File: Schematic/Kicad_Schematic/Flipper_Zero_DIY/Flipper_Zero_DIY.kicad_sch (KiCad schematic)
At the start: 0 parts

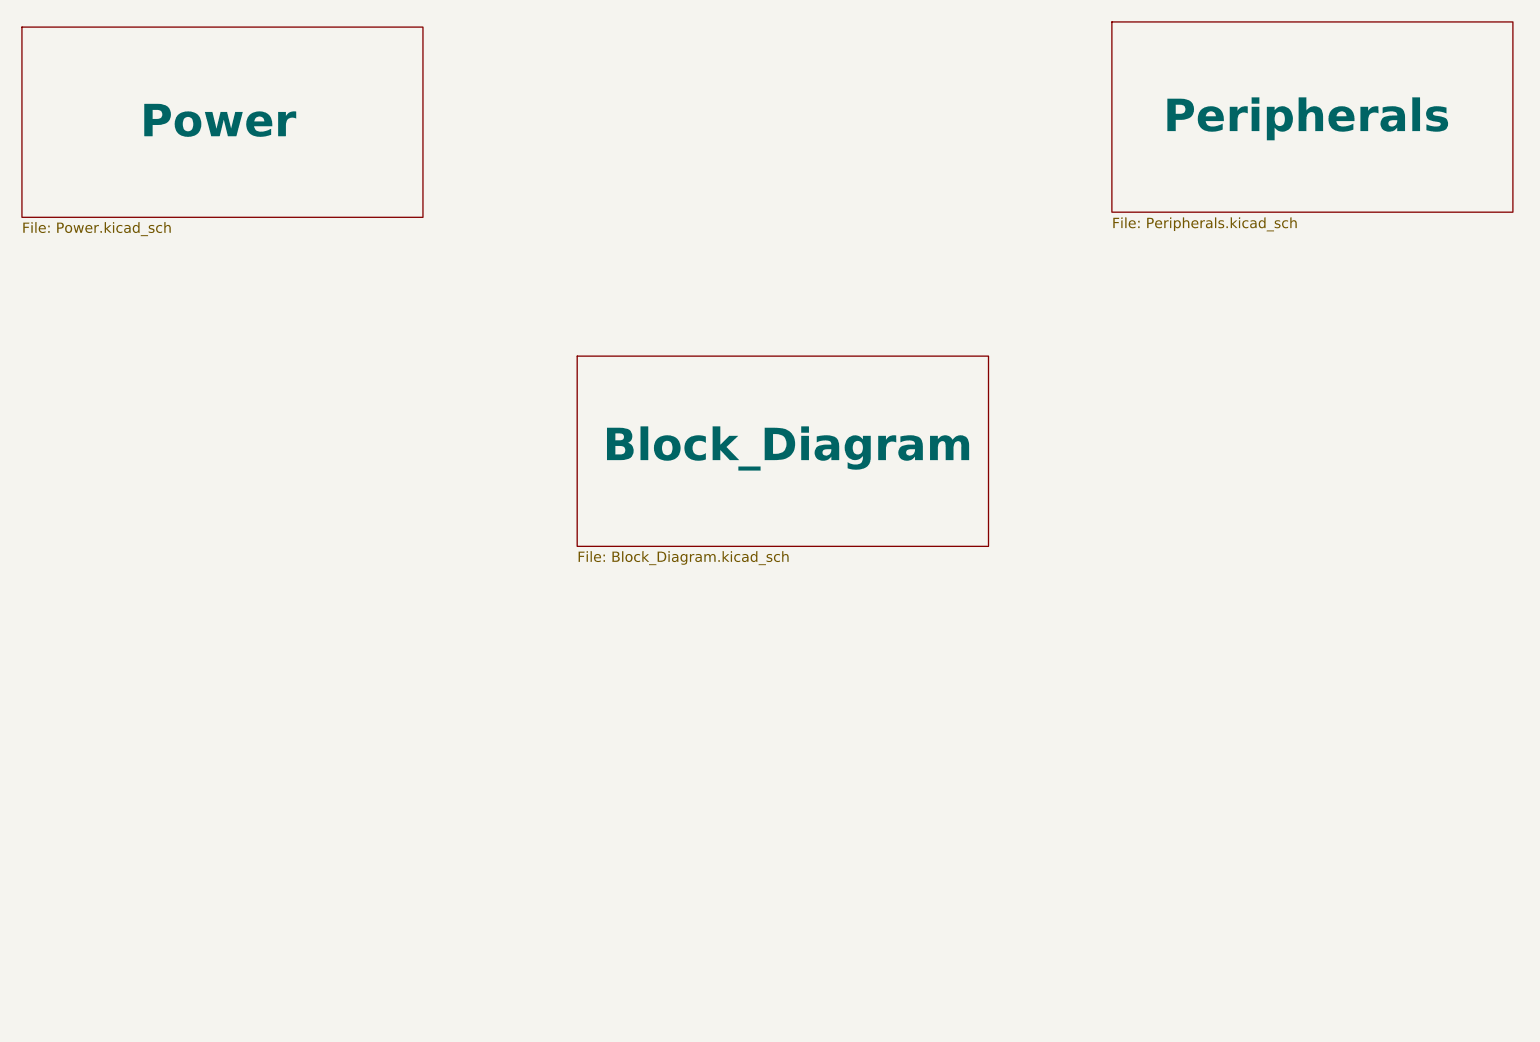
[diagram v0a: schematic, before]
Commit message: finished MCU schematic & new design of front shematic
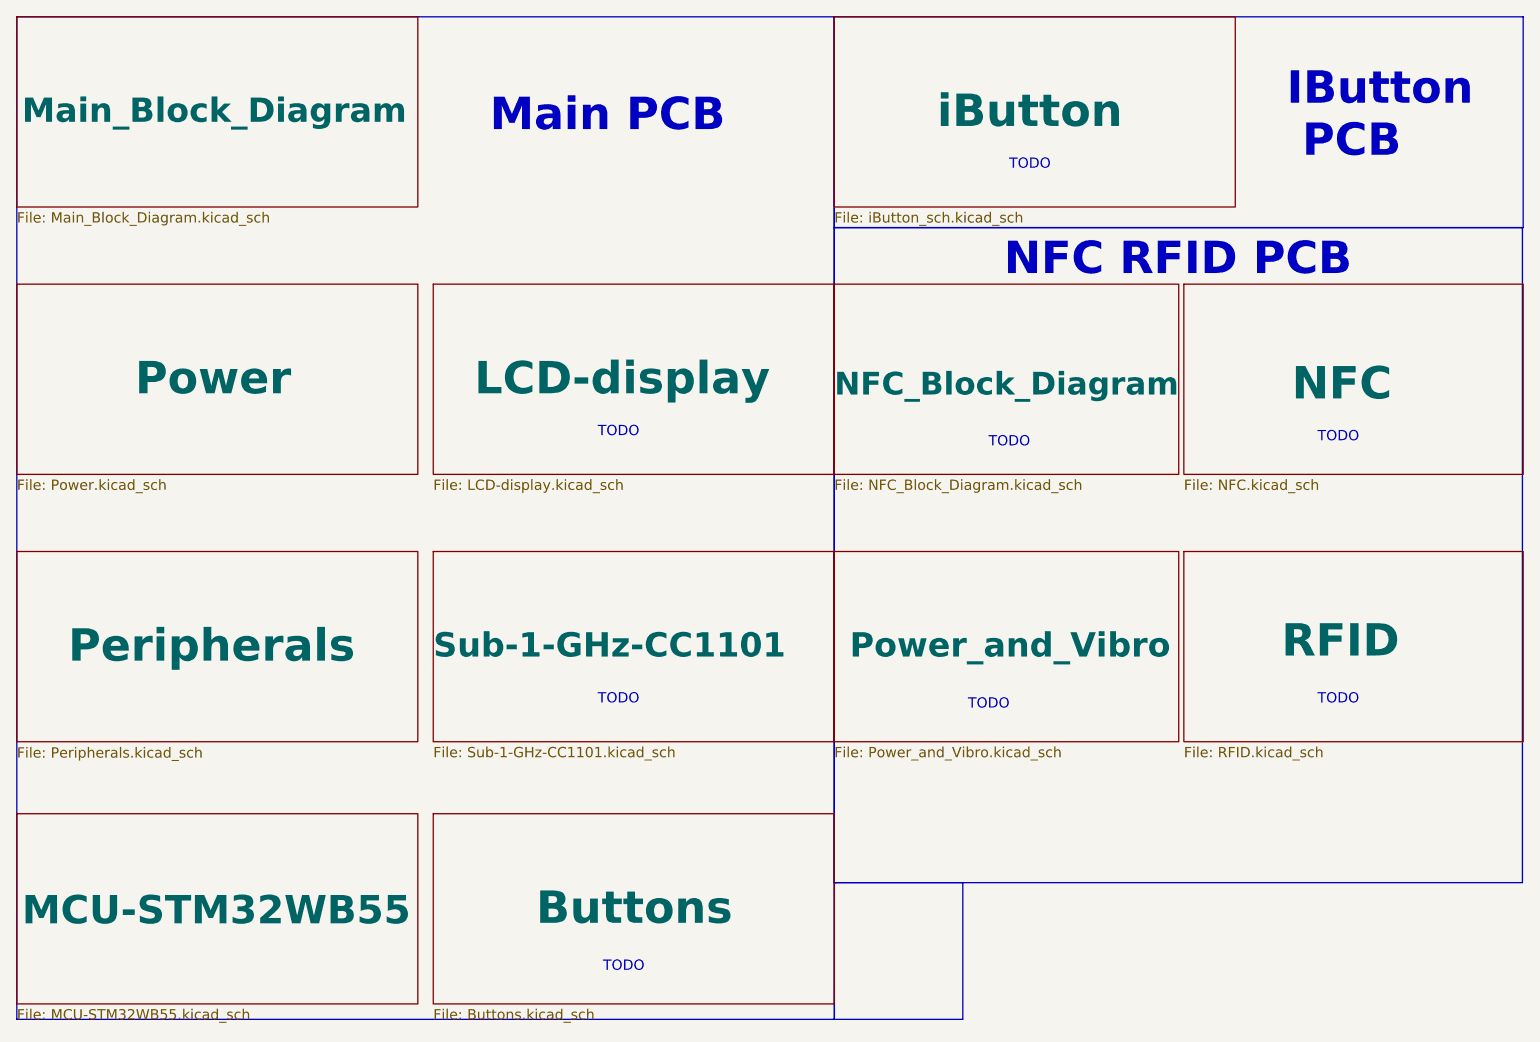
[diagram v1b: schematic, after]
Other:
- sheet Block_Diagram renamed Main_Block_Diagram
- added sheet Buttons (Buttons.kicad_sch)
- added sheet LCD-display (LCD-display.kicad_sch)
- added sheet MCU-STM32WB55 (MCU-STM32WB55.kicad_sch)
- added sheet NFC (NFC.kicad_sch)
- added sheet NFC_Block_Diagram (NFC_Block_Diagram.kicad_sch)
- added sheet Power_and_Vibro (Power_and_Vibro.kicad_sch)
- added sheet RFID (RFID.kicad_sch)
- added sheet Sub-1-GHz-CC1101 (Sub-1-GHz-CC1101.kicad_sch)
- added sheet iButton (iButton_sch.kicad_sch)
- sheet Main_Block_Diagram: file Block_Diagram.kicad_sch -> Main_Block_Diagram.kicad_sch
- note added: "IButton PCB"
- note added: "Main PCB"
- note added: "NFC RFID PCB"
- note added: "TODO"

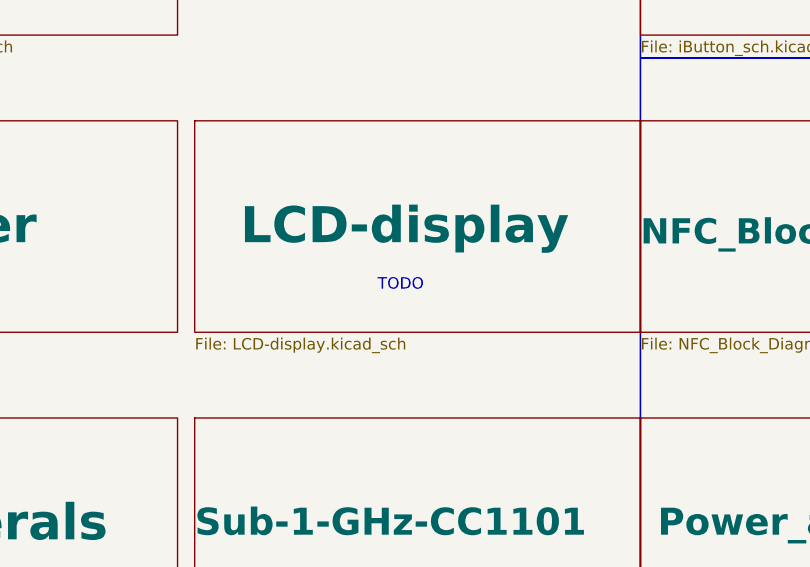
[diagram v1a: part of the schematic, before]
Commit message: Finished LCD-Display Schematic
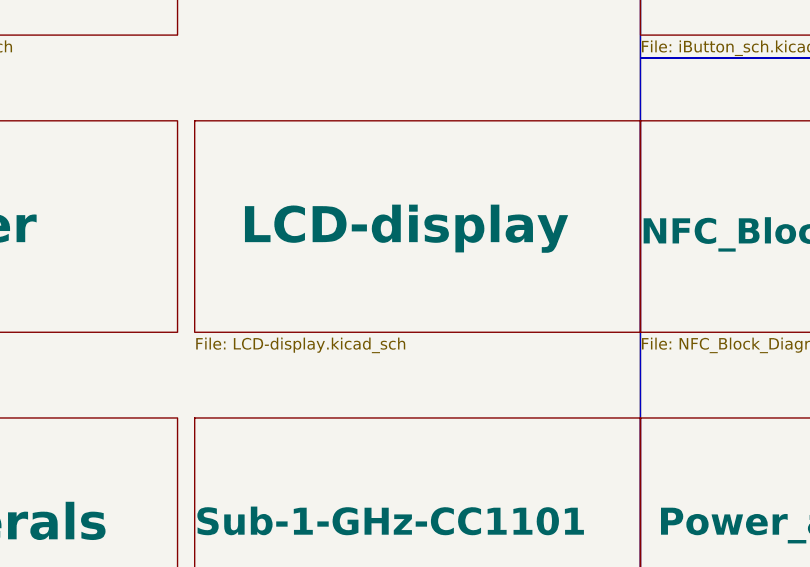
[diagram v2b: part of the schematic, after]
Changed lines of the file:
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@@
-    (effects (font (size 1.27 1.27)) (justify left bottom))
-  )
-  (text "TODO" (at 83.82 64.135 0)
     (effects (font (size 1.27 1.27)) (justify left bottom))
   )

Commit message: finished Su-1-GHz-CC1101
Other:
- company: Flipper Devices Inc. -> Originally from : Flipper Devices Inc.
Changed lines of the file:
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@@
     (title "Flipper Device DIY")
     (rev "13.F7B9C6")
-    (company "Flipper Devices Inc.")
+    (company "Originally from : Flipper Devices Inc.")
+    (comment 1 "DIY Version 1.0")
   )
   (rectangle (start 12.065 12.065) (end 113.03 135.89)
@@
     (effects (font (size 4 4) bold) (justify left bottom))
   )
-  (text "TODO" (at 83.82 97.155 0)
-    (effects (font (size 1.27 1.27)) (justify left bottom))
-  )
   (text "TODO" (at 132.08 65.405 0)

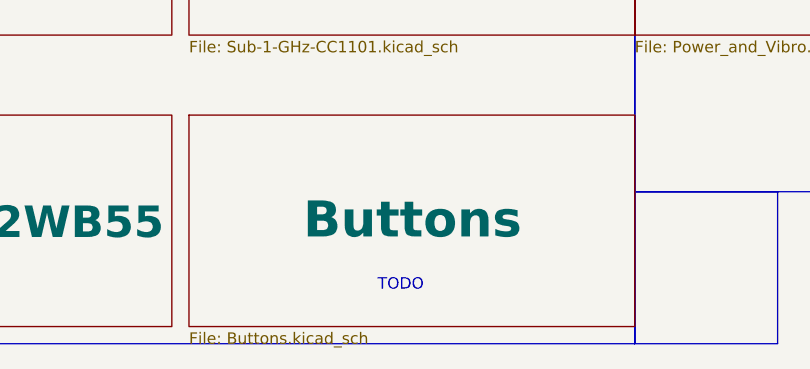
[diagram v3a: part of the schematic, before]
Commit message: Finished the button Schematic and so the main PCB Schematic :)
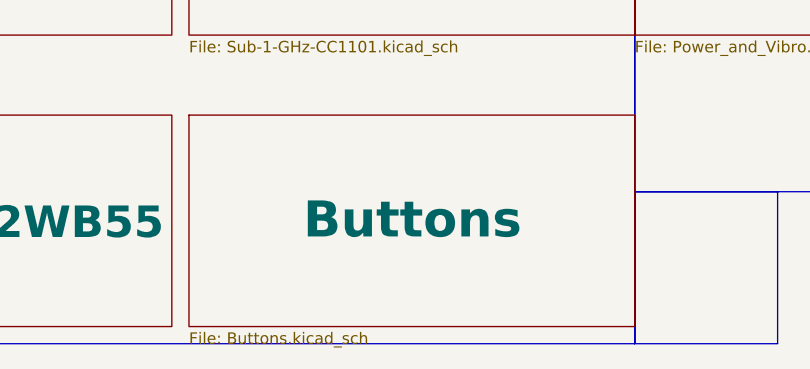
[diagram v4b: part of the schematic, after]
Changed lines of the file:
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@@
-    (effects (font (size 1.27 1.27)) (justify left bottom))
-  )
-  (text "TODO" (at 84.455 130.175 0)
     (effects (font (size 1.27 1.27)) (justify left bottom))
   )

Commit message: added all changes to the changelog
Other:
- added sheet change_log (change_log.kicad_sch)
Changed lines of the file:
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@@
     (comment 1 "DIY Version 1.0")
   )
-  (rectangle (start 12.065 12.065) (end 113.03 135.89)
-    (stroke (width 0) (type default))
+  (rectangle (start 12.065 12.065) (end 113.03 104.14)
+    (stroke (width -0.0001) (type default))
     (fill (type color) (color 255 243 84 0.46))
   )
@@
     (stroke (width 0) (type default))
     (fill (type color) (color 255 83 46 0.44))
+  )
+  (rectangle (start 33.02 31.115) (end 33.02 31.115)
+    (stroke (width 0) (type default))
+    (fill (type none))
+  )
+  (rectangle (start 12.065 104.14) (end 62.865 135.89)
+    (stroke (width -0.0001) (type default))
+    (fill (type color) (color 255 243 84 0.46))
+  )
+  (rectangle (start 62.865 104.14) (end 113.03 135.89)
+    (stroke (width 0) (type default))
+    (fill (type color) (color 110 255 142 0.46))
   )
   (image (at 120.9693 131.9377) (scale 1.48246)
@@
     (effects (font (size 1.27 1.27)) (justify left bottom))
   )
-  (text "Main PCB" (at 70.485 26.67 0)
+  (text "Main PCB" (at 47.625 43.815 0)
     (effects (font (size 4 4) (thickness 0.8) bold) (justify left bottom))
   )
@@
     )
   )
-  (sheet (at 63.5 45.085) (size 49.53 23.495)
-    (stroke (width 0.1524) (type solid))
-    (fill (color 0 132 0 0.4588))
-    (property "Sheetname" "LCD-display" (at 68.58 59.055 0)
-      (effects (font (size 4 4) bold) (justify left bottom))
-    )
-    (property "Sheetfile" "LCD-display.kicad_sch" (at 63.5 69.1646 0)
+  (sheet (at 12.065 45.72) (size 49.53 23.495)
+    (stroke (width 0.1524) (type solid))
+    (fill (color 0 132 0 0.4588))
+    (property "Sheetname" "LCD-display" (at 17.145 59.69 0)
+      (effects (font (size 4 4) bold) (justify left bottom))
+    )
+    (property "Sheetfile" "LCD-display.kicad_sch" (at 12.065 69.7996 0)
       (effects (font (size 1.27 1.27)) (justify left top))
     )
@@
     )
   )
-  (sheet (at 12.065 110.49) (size 49.53 23.495)
-    (stroke (width 0.1524) (type solid))
-    (fill (color 0 132 0 0.4588))
-    (property "Sheetname" "MCU-STM32WB55" (at 12.7 124.46 0)
+  (sheet (at 63.5 78.105) (size 49.53 23.495)
+    (stroke (width 0.1524) (type solid))
+    (fill (color 0 132 0 0.4588))
+    (property "Sheetname" "MCU-STM32WB55" (at 64.135 92.075 0)
       (effects (font (size 3.5 3.5) bold) (justify left bottom))
     )
-    (property "Sheetfile" "MCU-STM32WB55.kicad_sch" (at 12.065 134.5696 0)
+    (property "Sheetfile" "MCU-STM32WB55.kicad_sch" (at 63.5 102.1846 0)
       (effects (font (size 1.27 1.27)) (justify left top))
     )
@@
     )
   )
-  (sheet (at 12.065 45.085) (size 49.53 23.495)
-    (stroke (width 0.1524) (type solid))
-    (fill (color 0 132 0 0.4588))
-    (property "Sheetname" "Power" (at 26.67 59.055 0)
-      (effects (font (size 4 4) bold) (justify left bottom))
-    )
-    (property "Sheetfile" "Power.kicad_sch" (at 12.065 69.1646 0)
+  (sheet (at 63.5 12.065) (size 49.53 23.495)
+    (stroke (width 0.1524) (type solid))
+    (fill (color 0 132 0 0.4588))
+    (property "Sheetname" "Power" (at 78.105 26.035 0)
+      (effects (font (size 4 4) bold) (justify left bottom))
+    )
+    (property "Sheetfile" "Power.kicad_sch" (at 63.5 36.1446 0)
       (effects (font (size 1.27 1.27)) (justify left top))
     )
@@
     )
   )
-  (sheet (at 63.5 110.49) (size 49.53 23.495)
-    (stroke (width 0.1524) (type solid))
-    (fill (color 0 132 0 0.4588))
-    (property "Sheetname" "Buttons" (at 76.2 124.46 0)
-      (effects (font (size 4 4) bold) (justify left bottom))
-    )
-    (property "Sheetfile" "Buttons.kicad_sch" (at 63.5 134.5696 0)
+  (sheet (at 12.065 109.855) (size 49.53 23.495)
+    (stroke (width 0.1524) (type solid))
+    (fill (color 0 132 0 0.4588))
+    (property "Sheetname" "Buttons" (at 24.765 123.825 0)
+      (effects (font (size 4 4) bold) (justify left bottom))
+    )
+    (property "Sheetfile" "Buttons.kicad_sch" (at 12.065 133.9346 0)
       (effects (font (size 1.27 1.27)) (justify left top))
     )
@@
     )
   )
-  (sheet (at 63.5 78.105) (size 49.53 23.495)
-    (stroke (width 0.1524) (type solid))
-    (fill (color 0 132 0 0.4588))
-    (property "Sheetname" "Sub-1-GHz-CC1101" (at 63.5 91.44 0)
+  (sheet (at 12.065 78.105) (size 49.53 23.495)
+    (stroke (width 0.1524) (type solid))
+    (fill (color 0 132 0 0.4588))
+    (property "Sheetname" "Sub-1-GHz-CC1101" (at 12.065 91.44 0)
       (effects (font (size 3 3) bold) (justify left bottom))
     )
-    (property "Sheetfile" "Sub-1-GHz-CC1101.kicad_sch" (at 63.5 102.1846 0)
+    (property "Sheetfile" "Sub-1-GHz-CC1101.kicad_sch" (at 12.065 102.1846 0)
       (effects (font (size 1.27 1.27)) (justify left top))
     )
@@
     )
   )
-  (sheet (at 12.065 78.105) (size 49.53 23.495)
-    (stroke (width 0.1524) (type solid))
-    (fill (color 0 132 0 0.4588))
-    (property "Sheetname" "Peripherals" (at 18.415 92.075 0)
-      (effects (font (size 4 4) bold) (justify left bottom))
-    )
-    (property "Sheetfile" "Peripherals.kicad_sch" (at 12.065 102.235 0)
-      (effects (font (size 1.27 1.27)) (justify left top))
-    )
+  (sheet (at 63.5 109.855) (size 49.53 23.495)
+    (stroke (width 0.1524) (type solid))
+    (fill (color 0 132 0 0.4588))
+    (property "Sheetname" "change_log" (at 72.39 123.825 0)
+      (effects (font (size 3.5 3.5) bold) (justify left bottom))
+    )
+    (property "Sheetfile" "change_log.kicad_sch" (at 63.5 133.9346 0)
+      (effects (font (size 1.27 1.27)) (justify left top))
+    )
+    (instances
+      (project "Flipper_Zero_DIY"
+        (path "/6fd3b1c7-f4ee-4f40-ae71-a0439f037db8" (page "14"))
+      )
+    )
+  )
+  (sheet (at 63.5 45.085) (size 49.53 23.495)
+    (stroke (width 0.1524) (type solid))
+    (fill (color 0 132 0 0.4588))
+    (property "Sheetname" "Peripherals" (at 69.85 59.055 0)
+      (effects (font (size 4 4) bold) (justify left bottom))
+    )
+    (property "Sheetfile" "Peripherals.kicad_sch" (at 63.5 69.215 0)
+      (effects (font (size 1.27 1.27)) (justify left top))
+    )

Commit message: finished iBtn PCB
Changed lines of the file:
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@@
     (effects (font (size 4 4) bold) (justify left bottom))
-  )
-  (text "TODO" (at 134.62 31.115 0)
-    (effects (font (size 1.27 1.27)) (justify left bottom))
   )
   (text "Main PCB" (at 47.625 43.815 0)

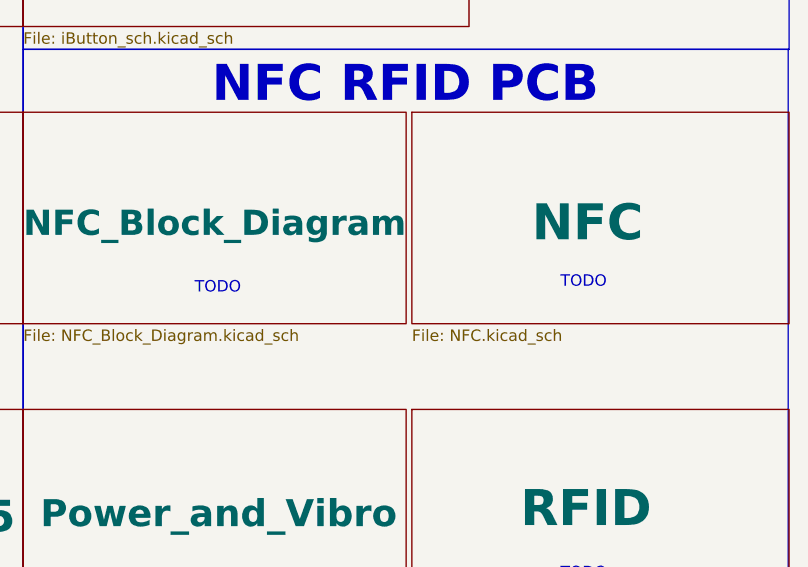
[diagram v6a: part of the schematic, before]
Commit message: finished NFC_RFID-Blockdia and NFC Schematic
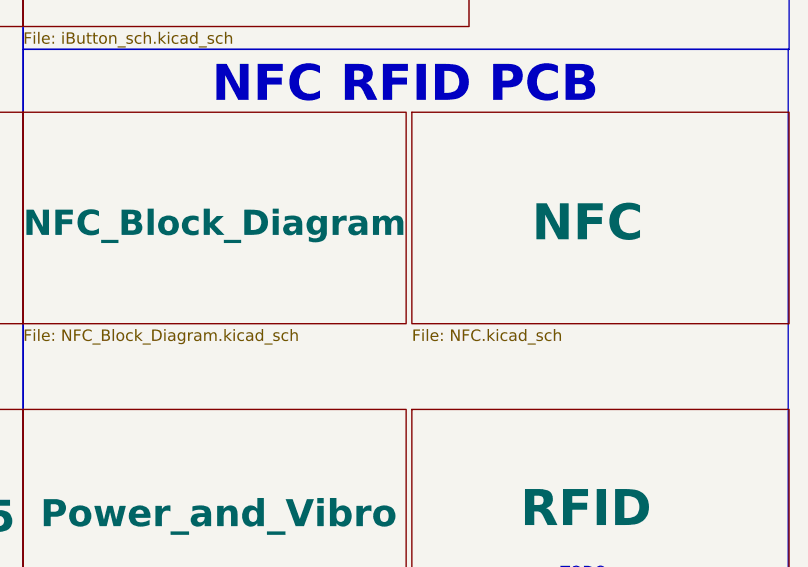
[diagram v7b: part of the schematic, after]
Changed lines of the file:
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@@
-    (effects (font (size 1.27 1.27)) (justify left bottom))
-  )
-  (text "TODO" (at 172.72 64.77 0)
     (effects (font (size 1.27 1.27)) (justify left bottom))
   )
@@
     (effects (font (size 4 4) bold) (justify left bottom))
   )
-  (text "TODO" (at 132.08 65.405 0)
-    (effects (font (size 1.27 1.27)) (justify left bottom))
-  )
   (text "TODO" (at 172.72 97.155 0)
